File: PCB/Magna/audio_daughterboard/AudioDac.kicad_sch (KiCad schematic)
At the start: 25 parts, among them U501 CS4344, U602 NE5532

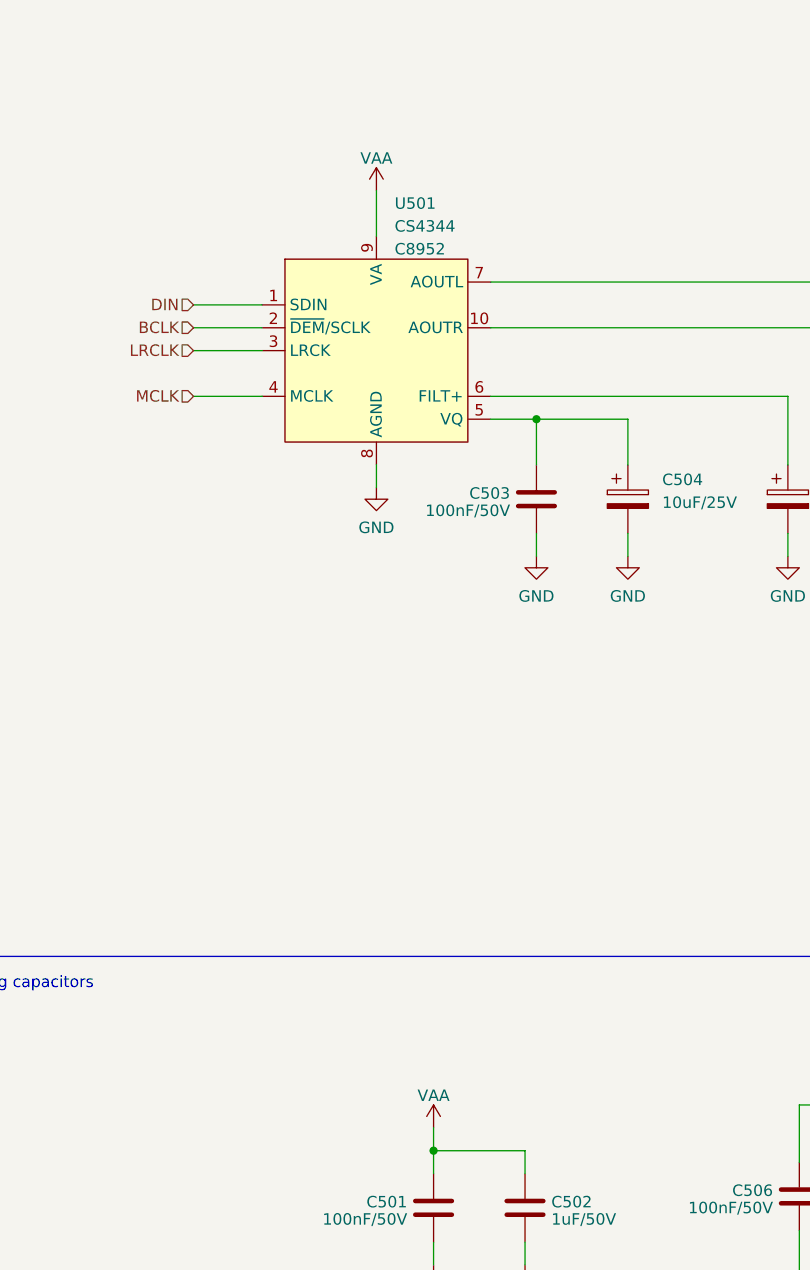
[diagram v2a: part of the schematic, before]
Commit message: Start of redesign of Audio board
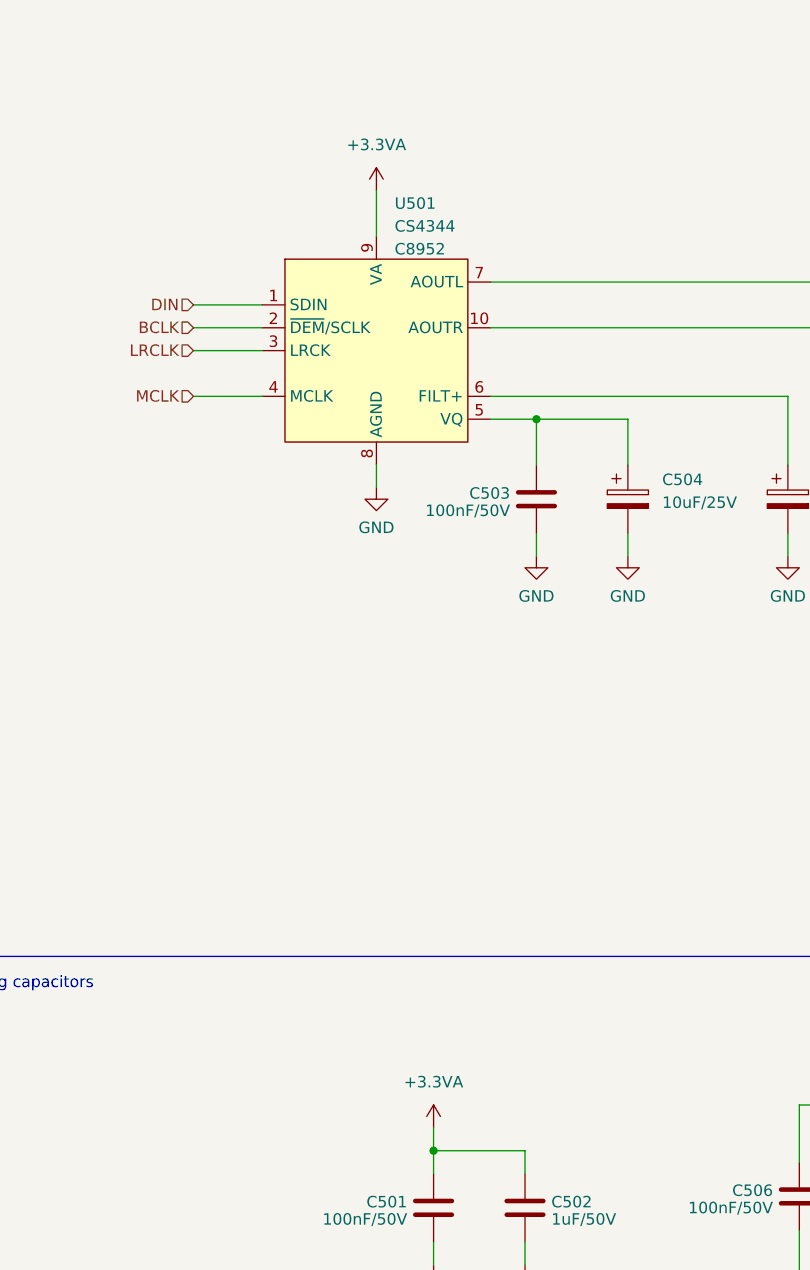
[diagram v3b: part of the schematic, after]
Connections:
- net VAA: no longer C501.1, C502.1, U501.9 (VA)
- new net +3.3VA: C501.1, C502.1, U501.9 (VA)
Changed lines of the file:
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@@
+    )
+  )
+  (symbol (lib_id "power:+3.3VA") (at 71.12 158.75 0) (unit 1)
+    (in_bom yes) (on_board yes) (dnp no) (fields_autoplaced)
+    (property "Reference" "#PWR0501" (at 71.12 162.56 0)
+      (effects (font (size 1.27 1.27)) hide)
+    )
+    (property "Value" "+3.3VA" (at 71.12 153.67 0)
+      (effects (font (size 1.27 1.27)))
+    )
+    (property "Footprint" "" (at 71.12 158.75 0)
+      (effects (font (size 1.27 1.27)) hide)
+    )
+    (property "Datasheet" "" (at 71.12 158.75 0)
+      (effects (font (size 1.27 1.27)) hide)
+    )
+    (pin "1")
+    (instances
+      (project "Audio_daughterboard"
+        (path "/1eadd930-2484-4c28-b568-78e6454e7f52/396242ef-243f-440f-bcad-6ad240970fd6"
+          (reference "#PWR0501") (unit 1)
+        )
+        (path "/1eadd930-2484-4c28-b568-78e6454e7f52/0f70dfcf-faa8-4745-8ffb-98640ceeb78a"
+          (reference "#PWR0401") (unit 1)
+        )
+      )
     )
   )
@@
     )
   )
-  (symbol (lib_id "power:VAA") (at 64.77 54.61 0) (unit 1)
-    (in_bom yes) (on_board yes) (dnp no) (fields_autoplaced)
-    (property "Reference" "#PWR0501" (at 64.77 58.42 0)
-      (effects (font (size 1.27 1.27)) hide)
-    )
-    (property "Value" "VAA" (at 64.77 51.0342 0)
+  (symbol (lib_id "power:+3.3VA") (at 64.77 54.61 0) (unit 1)
+    (in_bom yes) (on_board yes) (dnp no) (fields_autoplaced)
+    (property "Reference" "#PWR0403" (at 64.77 58.42 0)
+      (effects (font (size 1.27 1.27)) hide)
+    )
+    (property "Value" "+3.3VA" (at 64.77 49.53 0)
       (effects (font (size 1.27 1.27)))
     )
@@
     (pin "1")
     (instances
-      (project "Magna"
-        (path "/1469ea1f-a157-49dc-a369-2d42fa17695d/22259812-9e7f-4230-9f2b-a9eb5ce4aaf1/0f70dfcf-faa8-4745-8ffb-98640ceeb78a"
-          (reference "#PWR0501") (unit 1)
-        )
-        (path "/1469ea1f-a157-49dc-a369-2d42fa17695d/22259812-9e7f-4230-9f2b-a9eb5ce4aaf1/396242ef-243f-440f-bcad-6ad240970fd6"
-          (reference "#PWR0601") (unit 1)
-        )
-      )
-      (project "Audio_daughterboard"
-        (path "/1eadd930-2484-4c28-b568-78e6454e7f52/0f70dfcf-faa8-4745-8ffb-98640ceeb78a"
-          (reference "#PWR0401") (unit 1)
-        )
-        (path "/1eadd930-2484-4c28-b568-78e6454e7f52/396242ef-243f-440f-bcad-6ad240970fd6"
-          (reference "#PWR0501") (unit 1)
+      (project "Audio_daughterboard"
+        (path "/1eadd930-2484-4c28-b568-78e6454e7f52/0f70dfcf-faa8-4745-8ffb-98640ceeb78a"
+          (reference "#PWR0403") (unit 1)
+        )
+        (path "/1eadd930-2484-4c28-b568-78e6454e7f52/396242ef-243f-440f-bcad-6ad240970fd6"
+          (reference "#PWR0503") (unit 1)
         )
       )
@@
         )
       )
-    )
-  )
-  (symbol (lib_id "power:VAA") (at 71.12 158.75 0) (unit 1)
-    (in_bom yes) (on_board yes) (dnp no) (fields_autoplaced)
-    (property "Reference" "#PWR0503" (at 71.12 162.56 0)
-      (effects (font (size 1.27 1.27)) hide)
-    )
-    (property "Value" "VAA" (at 71.12 155.1742 0)
-      (effects (font (size 1.27 1.27)))
-    )
-    (property "Footprint" "" (at 71.12 158.75 0)
-      (effects (font (size 1.27 1.27)) hide)
-    )
-    (property "Datasheet" "" (at 71.12 158.75 0)
-      (effects (font (size 1.27 1.27)) hide)
-    )
-    (pin "1")
-    (instances
-      (project "Magna"
-        (path "/1469ea1f-a157-49dc-a369-2d42fa17695d/22259812-9e7f-4230-9f2b-a9eb5ce4aaf1/0f70dfcf-faa8-4745-8ffb-98640ceeb78a"
-          (reference "#PWR0503") (unit 1)
-        )
-        (path "/1469ea1f-a157-49dc-a369-2d42fa17695d/22259812-9e7f-4230-9f2b-a9eb5ce4aaf1/396242ef-243f-440f-bcad-6ad240970fd6"
-          (reference "#PWR0603") (unit 1)
-        )
-      )
-      (project "Audio_daughterboard"
-        (path "/1eadd930-2484-4c28-b568-78e6454e7f52/0f70dfcf-faa8-4745-8ffb-98640ceeb78a"
-          (reference "#PWR0403") (unit 1)
-        )
-        (path "/1eadd930-2484-4c28-b568-78e6454e7f52/396242ef-243f-440f-bcad-6ad240970fd6"
-          (reference "#PWR0503") (unit 1)
-        )
-      )

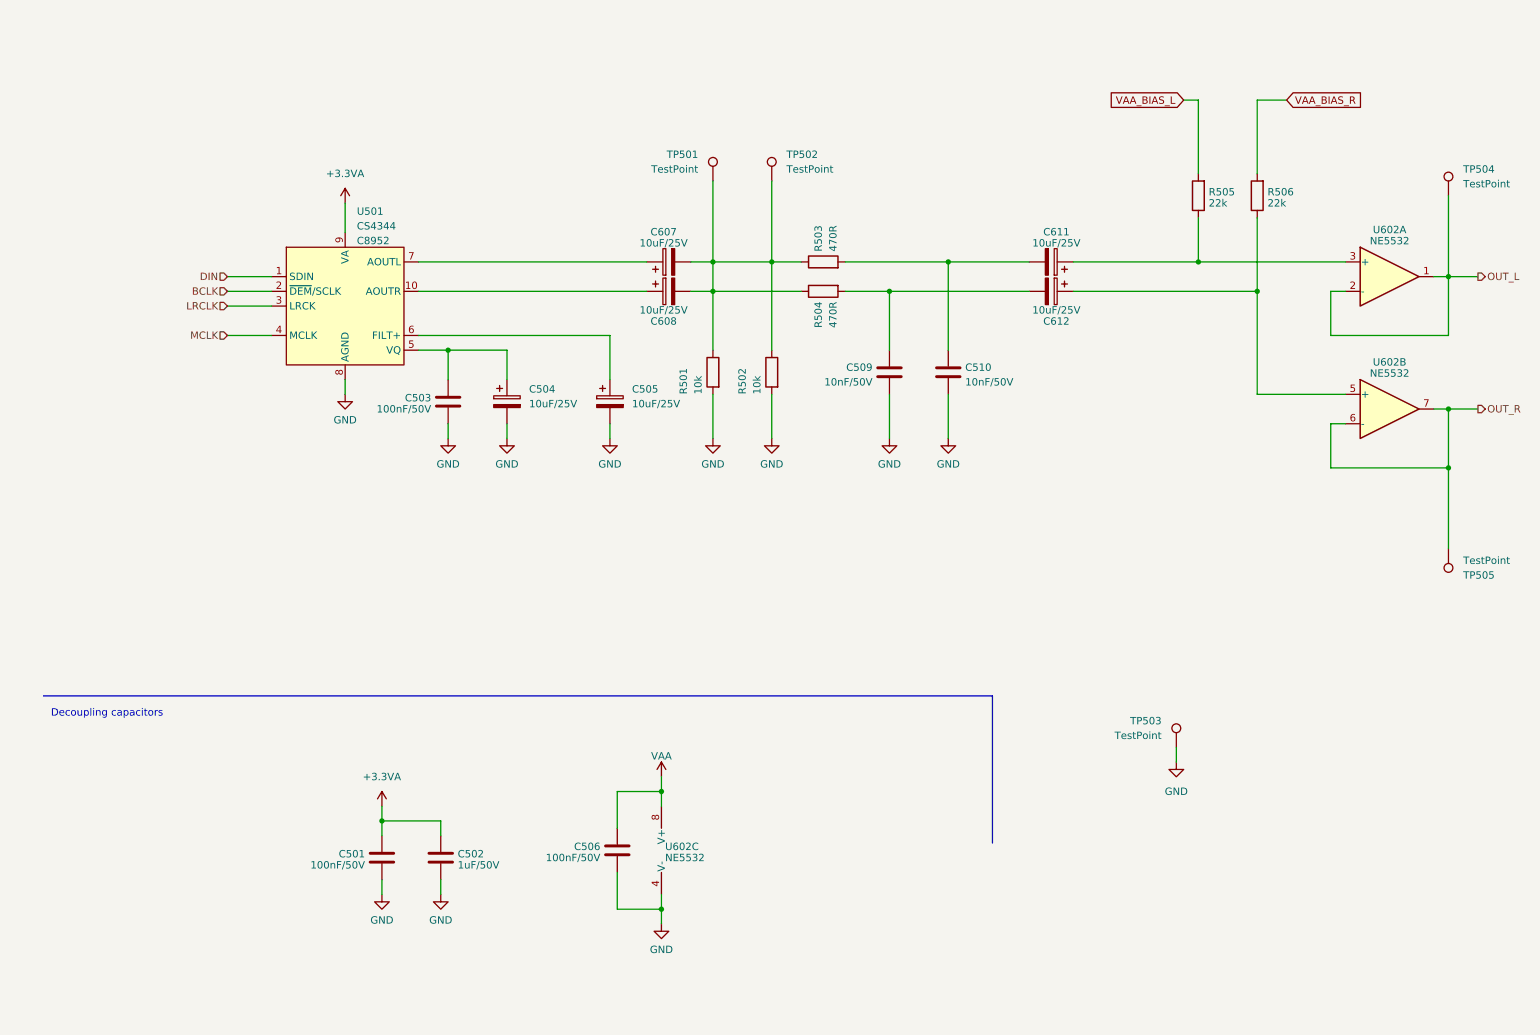
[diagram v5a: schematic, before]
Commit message: Change ADC and add MCU for IO control
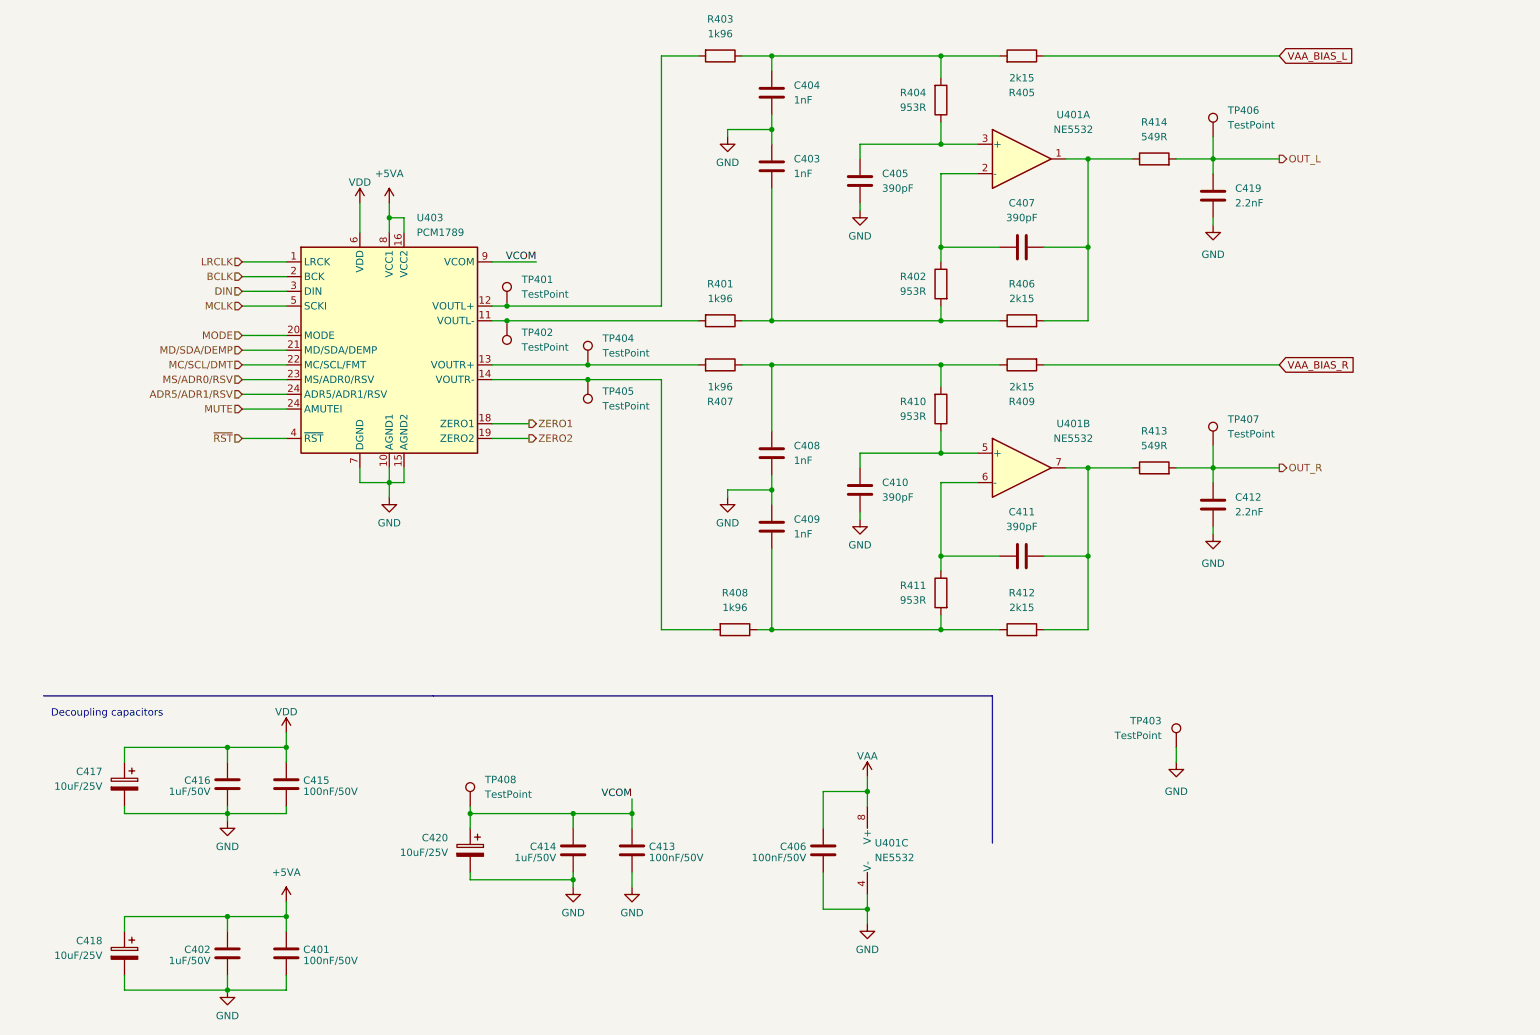
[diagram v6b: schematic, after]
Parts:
- removed C503: 100nF/50V, Capacitor_SMD:C_0805_2012Metric_Pad1.18x1.45mm_HandSolder, symbol Device:C
- removed C504, C505, C607, C608, C611, C612: 10uF/25V, Capacitor_SMD:CP_Elec_4x5.8, symbol Device:C_Polarized
- removed C509, C510: 10nF/50V, Capacitor_SMD:C_0805_2012Metric_Pad1.18x1.45mm_HandSolder, symbol Device:C
- removed R501, R502: 10k, Resistor_SMD:R_0805_2012Metric_Pad1.20x1.40mm_HandSolder, symbol Device:R
- removed R503, R504: 470R, Resistor_SMD:R_0805_2012Metric_Pad1.20x1.40mm_HandSolder, symbol Device:R
- removed R505, R506: 22k, Resistor_SMD:R_0805_2012Metric_Pad1.20x1.40mm_HandSolder, symbol Device:R
- removed TP501, TP502, TP504, TP505: TestPoint, TestPoint:TestPoint_Keystone_5005-5009_Compact, symbol Connector:TestPoint
- removed U501: CS4344, Package_SO:MSOP-10_3x3mm_P0.5mm, symbol Skrooter_symbols:CS4344
- removed U602: NE5532, Package_SO:SOIC-8_3.9x4.9mm_P1.27mm, symbol Amplifier_Operational:NE5532
- added C403, C404, C408, C409: 1nF, symbol Device:C
- added C405, C407, C410, C411: 390pF, symbol Device:C
- added C412, C419: 2.2nF, symbol Device:C
- added C413, C415: 100nF/50V, Capacitor_SMD:C_0805_2012Metric_Pad1.18x1.45mm_HandSolder, symbol Device:C
- added C414, C416: 1uF/50V, Capacitor_SMD:C_0805_2012Metric_Pad1.18x1.45mm_HandSolder, symbol Device:C
- added C417, C418, C420: 10uF/25V, Capacitor_SMD:CP_Elec_4x5.8, symbol Device:C_Polarized
- added R401, R403, R407, R408: 1k96, symbol Device:R
- added R402, R404, R410, R411: 953R, symbol Device:R
- added R405, R406, R409, R412: 2k15, symbol Device:R
- added R413, R414: 549R, symbol Device:R
- added TP401, TP402, TP404, TP405, TP406, TP407, TP408: TestPoint, symbol Connector:TestPoint
- added U401: NE5532, symbol Amplifier_Operational:NE5532
- added U403: PCM1789, Package_SO:TSSOP-24_4.4x7.8mm_P0.65mm, symbol Skrooter_symbols:PCM1789
- renumbered C501 to C401, C502 to C402, C506 to C406, TP503 to TP403
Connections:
- net BCLK: now also U403.2 (BCK)
- net DIN: now also U403.3 (DIN)
- net GND: now also C403.1, C404.2, C405.2, C408.2, C409.1, C410.2, C412.1, C413.2, C414.2, C415.2, C416.2, C417.2, C418.2, C419.1, C420.2, U401.4 (V-), U403.10 (AGND1), U403.15 (AGND2), U403.7 (DGND)
- net LRCLK: now also U403.1 (LRCK)
- net MCLK: now also U403.5 (SCKI)
- net OUT_L: now also C419.2, R414.2, TP406.1
- net OUT_R: now also C412.2, R413.2, TP407.1
- net VAA: now also U401.8 (V+)
- net VAA_BIAS_L: now also R405.1
- net VAA_BIAS_R: now also R409.2
- net +3.3VA renamed +5VA
- net +5VA: now also C418.1, U403.16 (VCC2), U403.8 (VCC1)
- new net: C407.2, R406.2, R414.1, U401.1
- new net: C407.1, R402.1, U401.2 (-)
- new net: C405.1, R404.1, U401.3 (+)
- new net: R403.2, TP401.1, U403.12 (VOUTL+)
- new net: C410.1, R410.1, U401.5 (+)
- new net: C408.1, R407.1, R409.1, R410.2
- new net: R408.2, TP405.1, U403.14 (VOUTR-)
- new net: C411.2, R412.2, R413.1, U401.7
- new net: C403.2, R401.1, R402.2, R406.1
- new net: C404.1, R403.1, R404.2, R405.2
- new net: R401.2, TP402.1, U403.11 (VOUTL-)
- new net: R407.2, TP404.1, U403.13 (VOUTR+)
- new net: C411.1, R411.1, U401.6 (-)
- new net: C409.2, R408.1, R411.2, R412.1
- new net ADR5/ADR1/RSV: U403.24 (AMUTEI)
- new net MC/SCL/DMT: U403.22 (MC/SCL/FMT)
- new net MD/SDA/DEMP: U403.21 (MD/SDA/DEMP)
- new net MODE: U403.20 (MODE)
- new net MS/ADR0/RSV: U403.23 (MS/ADR0/RSV)
- new net MUTE: U403.24 (AMUTEI)
- new net VCOM: C413.1, C414.1, C420.1, TP408.1, U403.9 (VCOM)
- new net VDD: C415.1, C416.1, C417.1, U403.6 (VDD)
- new net ZERO1: U403.18 (ZERO1)
- new net ZERO2: U403.19 (ZERO2)
- new net ~{RST}: U403.4 (~{RST})
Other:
- moved on the sheet: C401, C402, C406
